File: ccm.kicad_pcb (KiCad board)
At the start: 2 copper layers, 80.1 x 75.2 mm, 24 parts, among them J3 Conn_01x04_Socket, J4 Conn_01x04_Socket, J5 Conn_01x04_Socket, J6 Conn_01x02_Socket, J7 Conn_01x02_Socket, J8 Conn_01x04_Socket, U1 Teensy4.1, U2 LM1117DT-1.8, U3 SN65HVD230, U4 SN65HVD230

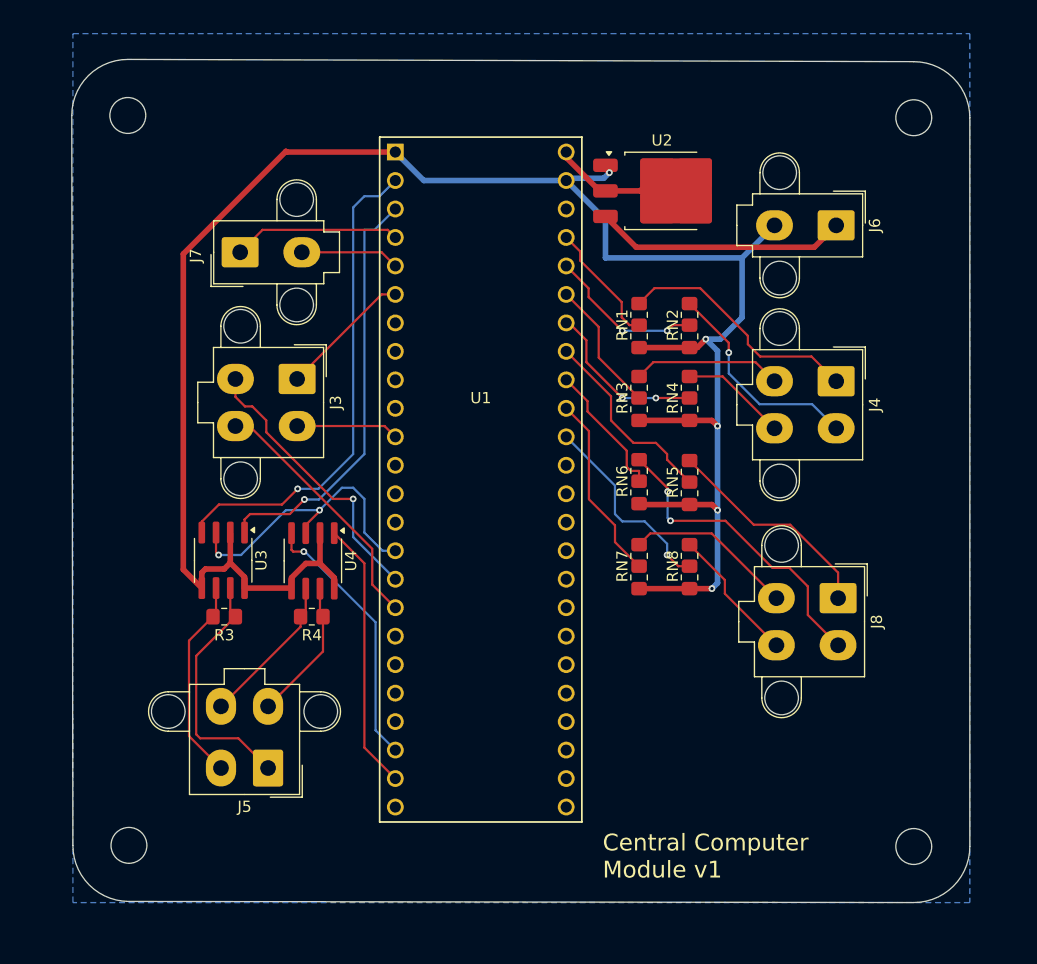
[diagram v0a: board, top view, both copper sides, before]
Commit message: add mosfet for brake light output and decoupling capacitors
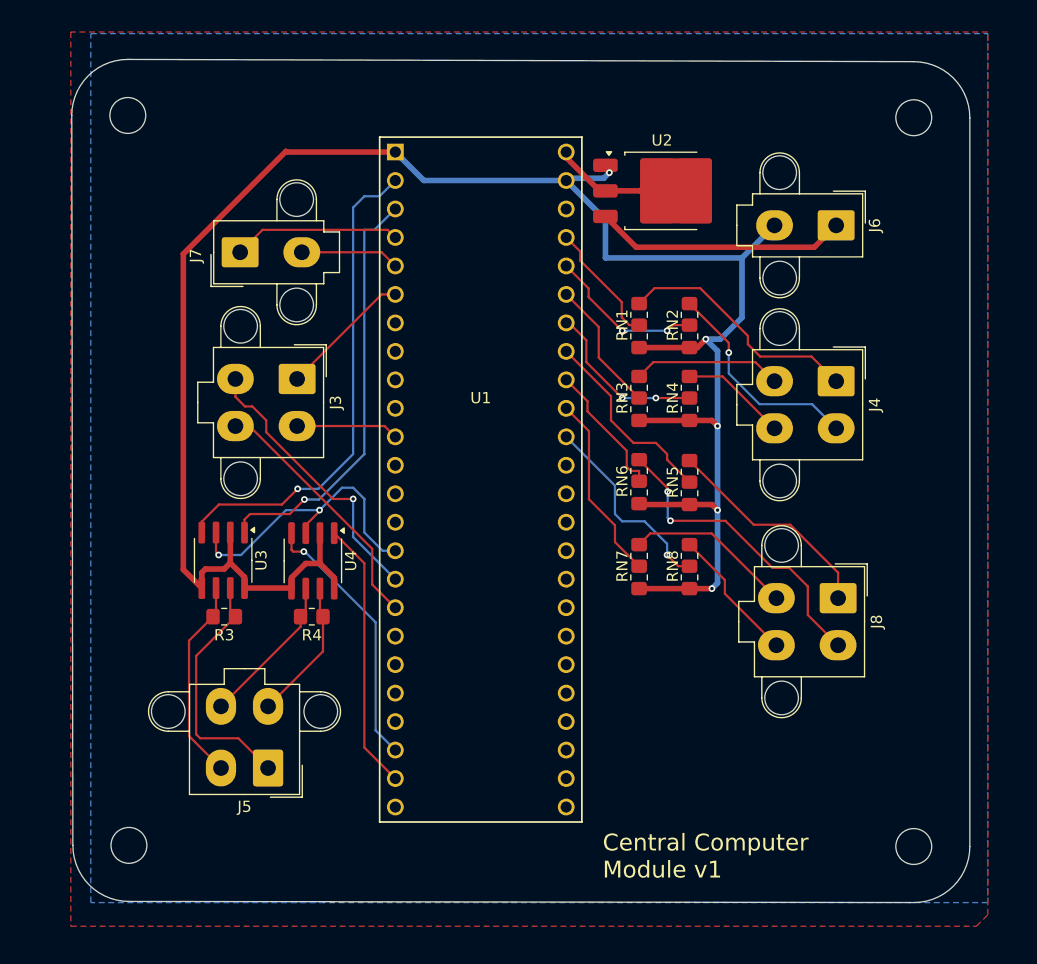
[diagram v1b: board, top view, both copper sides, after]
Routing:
- added copper zone on F.Cu, net GLV-
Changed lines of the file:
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@@
+		(net 2)
+		(net_name "GLV-")
+		(layer "F.Cu")
+		(hatch edge 0.5)
+		(priority 1)
+		(connect_pads
+			(clearance 0.5)
+		)
+		(min_thickness 0.25)
+		(filled_areas_thickness no)
+		(fill yes
+			(thermal_gap 0.5)
+			(thermal_bridge_width 0.5)
+		)
+		(polygon
+			(pts
+				(xy 108.816 59.356) (xy 108.816 139.112) (xy 189.588 139.112) (xy 190.604 138.096) (xy 190.604 59.356)
+			)
+		)
+	)
+	(zone
 		(net 2)
 		(net_name "GLV-")
@@
 		(polygon
 			(pts
-				(xy 109 59.5) (xy 189 59.5) (xy 189 137) (xy 109 137)
+				(xy 110.604 59.5) (xy 190.604 59.5) (xy 190.604 137) (xy 110.604 137)
 			)
 		)

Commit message: backup commit (no split termination or speaker amp)
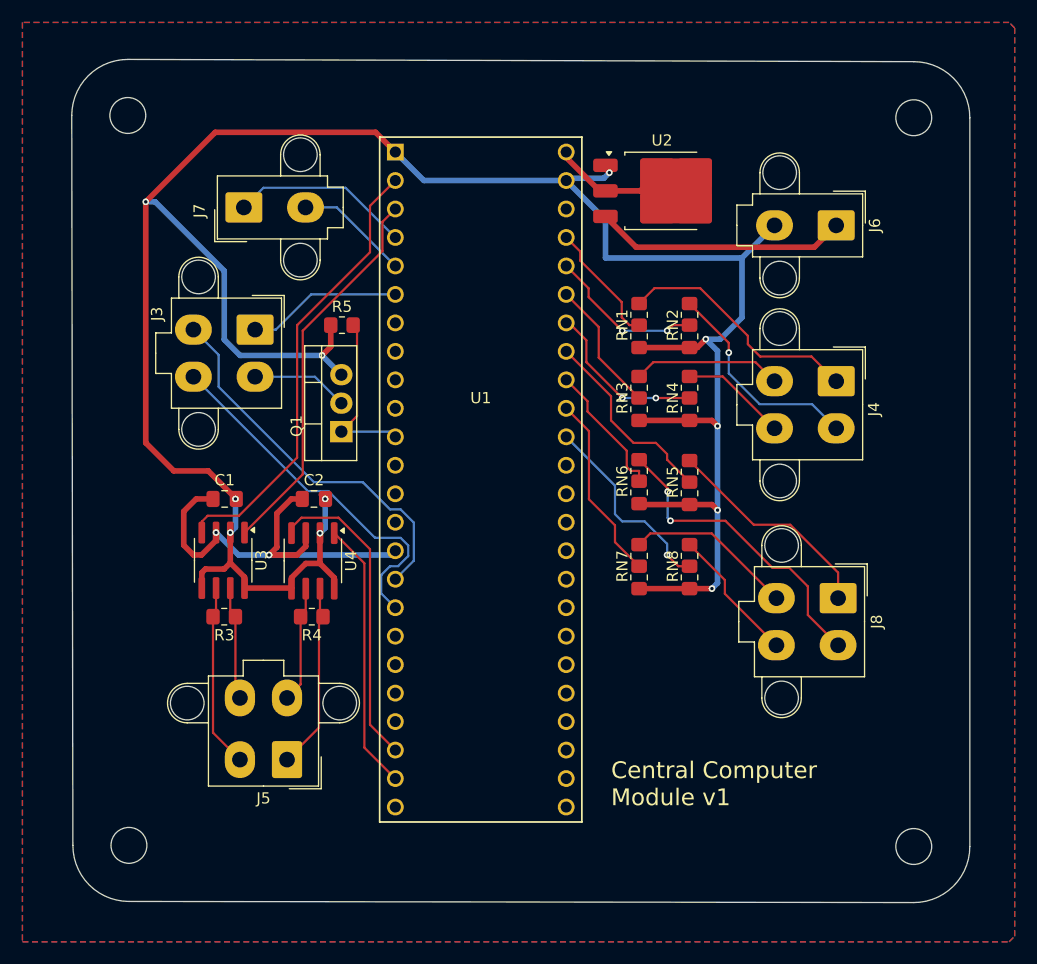
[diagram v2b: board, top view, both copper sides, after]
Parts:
- added C1: 100 nF, Capacitor_SMD:C_0805_2012Metric_Pad1.18x1.45mm_HandSolder, F.Cu at (122.5, 101.0)
- added C2: 100 nF, Capacitor_SMD:C_0805_2012Metric_Pad1.18x1.45mm_HandSolder, F.Cu at (130.5, 101.0)
- added Q1: IRLZ34N, Package_TO_SOT_THT:TO-220-3_Vertical, F.Cu at (132.9, 95.0)
- added R5: 10k, Resistor_SMD:R_0805_2012Metric_Pad1.20x1.40mm_HandSolder, F.Cu at (133.0, 85.5)
- U2: value LM1117DT-1.8 -> LM1117DT-5.0
- moved J3 5.78 mm to (125.2, 85.9)
- moved J7 4.01 mm to (124.2, 75.0)
- moved J5 1.85 mm to (128.1, 124.2)
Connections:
- J5 pad 1: CANH_1 -> CANH_2
- J5 pad 3: CANH_2 -> CANL_2
- J5 pad 4: CANL_2 -> CANH_1
- U1 pad 11: brake_light -> Net-(Q1-G)
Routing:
- net GLV-: track 181.9 -> 223.5 mm, vias 5 -> 11
- net Net-(Q1-G): track 0.00 -> 15.2 mm
- net CANH_1: track 22.3 -> 10.2 mm
- net +3.3V: track 27.0 -> 39.1 mm
- net i2c_SDA: track 22.8 -> 32.9 mm
- net i2c_SCL: track 25.2 -> 34.2 mm, vias 1 -> 0
- net CAN_RX_2: track 23.8 -> 27.9 mm, vias 1 -> 0
- net CANH_2: track 12.6 -> 16.7 mm
- net CAN_RX_1: track 43.7 -> 40.2 mm, vias 1 -> 0
- net CAN_TX_1: track 37.8 -> 34.4 mm, vias 1 -> 0
- net CANL_2: track 13.6 -> 10.4 mm
- net ready_to_drive_button: track 11.9 -> 13.8 mm
- net CANL_1: track 18.2 -> 16.4 mm
- net PWM_in_2: track 8.85 -> 10.2 mm
- net PWM_in_1: track 15.0 -> 16.1 mm

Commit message: changed voltage divider to use 2 resistors
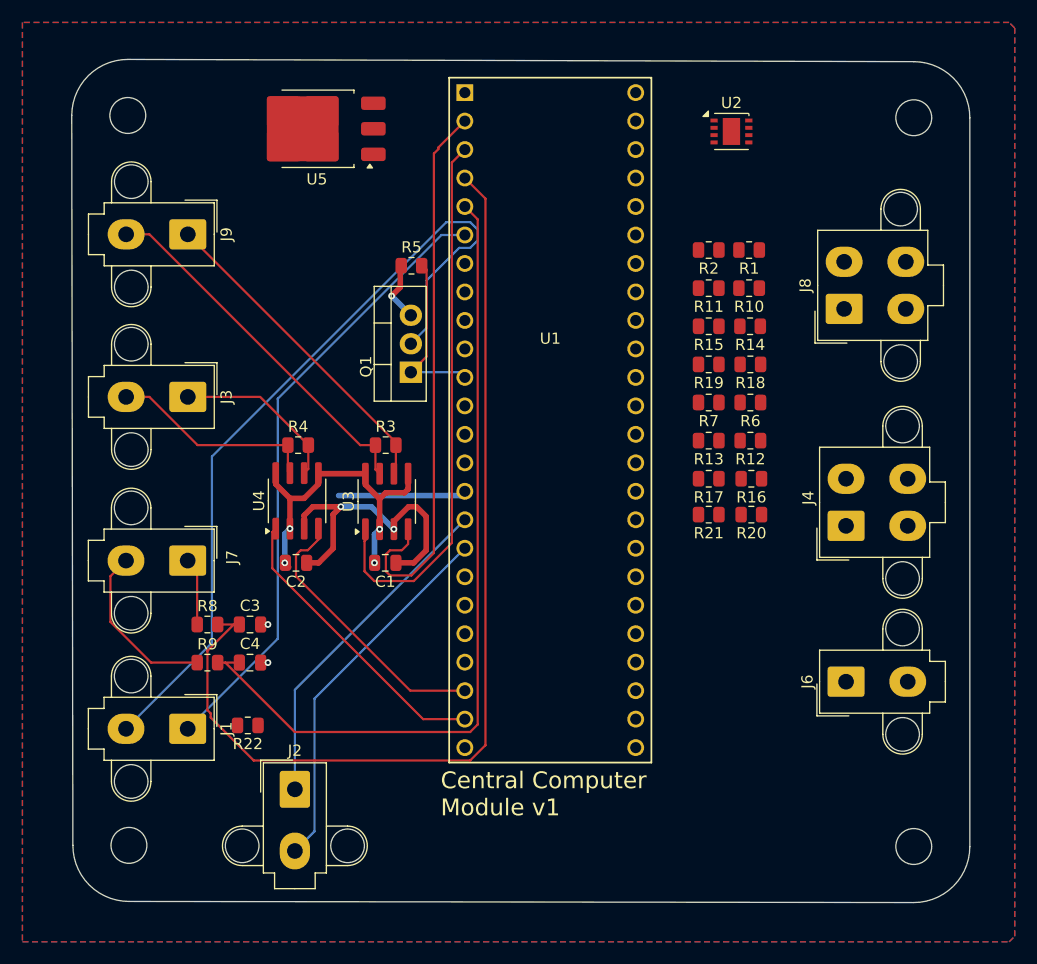
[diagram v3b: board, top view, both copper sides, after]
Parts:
- removed J5: Conn_01x04_Socket, Connector_Molex:Molex_Mini-Fit_Jr_5566-04A2_2x02_P4.20mm_Vertical
- removed RN1, RN2, RN3, RN4, RN5, RN6, RN7, RN8: VoltageDivider, voltagedivider:Voltage_Divider
- added C3: 0.01uF, Capacitor_SMD:C_0805_2012Metric, F.Cu at (124.8, 112.2)
- added C4: 0.01uF, Capacitor_SMD:C_0805_2012Metric, F.Cu at (124.8, 115.6)
- added J1: Conn_01x02_Socket, Connector_Molex:Molex_Mini-Fit_Jr_5566-02A2_2x01_P4.20mm_Vertical, F.Cu at (119.2, 121.5)
- added J2: Conn_01x02_Socket, Connector_Molex:Molex_Mini-Fit_Jr_5566-02A2_2x01_P4.20mm_Vertical, F.Cu at (128.8, 126.9)
- added J9: Conn_01x02_Socket, Connector_Molex:Molex_Mini-Fit_Jr_5566-02A2_2x01_P4.20mm_Vertical, F.Cu at (119.2, 77.4)
- added R1: 1k, Resistor_SMD:R_0805_2012Metric, F.Cu at (169.3, 78.8)
- added R10: 1k, Resistor_SMD:R_0805_2012Metric, F.Cu at (169.3, 82.2)
- added R11: 1k, Resistor_SMD:R_0805_2012Metric, F.Cu at (165.7, 82.2)
- added R12: 1k, Resistor_SMD:R_0805_2012Metric, F.Cu at (169.4, 95.8)
- added R13: 1k, Resistor_SMD:R_0805_2012Metric, F.Cu at (165.7, 95.8)
- added R14: 1k, Resistor_SMD:R_0805_2012Metric, F.Cu at (169.4, 85.6)
- added R15: 1k, Resistor_SMD:R_0805_2012Metric, F.Cu at (165.7, 85.6)
- added R16: 1k, Resistor_SMD:R_0805_2012Metric, F.Cu at (169.5, 99.2)
- added R17: 1k, Resistor_SMD:R_0805_2012Metric, F.Cu at (165.7, 99.2)
- added R18: 1k, Resistor_SMD:R_0805_2012Metric, F.Cu at (169.4, 89.0)
- added R19: 1k, Resistor_SMD:R_0805_2012Metric, F.Cu at (165.7, 89.0)
- added R2: 1k, Resistor_SMD:R_0805_2012Metric, F.Cu at (165.7, 78.8)
- added R20: 1k, Resistor_SMD:R_0805_2012Metric, F.Cu at (169.5, 102.4)
- added R21: 1k, Resistor_SMD:R_0805_2012Metric, F.Cu at (165.7, 102.4)
- added R22: 10k, Resistor_SMD:R_0805_2012Metric, F.Cu at (124.6, 121.2)
- added R6: 1k, Resistor_SMD:R_0805_2012Metric, F.Cu at (169.4, 92.4)
- added R7: 1k, Resistor_SMD:R_0805_2012Metric, F.Cu at (165.7, 92.4)
- added R8: 10, Resistor_SMD:R_0805_2012Metric, F.Cu at (121.0, 112.2)
- added R9: 10, Resistor_SMD:R_0805_2012Metric, F.Cu at (121.0, 115.6)
- added U5: LM1117DT-5.0, Package_TO_SOT_SMD:TO-252-3_TabPin2, F.Cu at (130.8, 68.0)
- C1, C2: footprint Capacitor_SMD:C_0805_2012Metric_Pad1.18x1.45mm_HandSolder -> Capacitor_SMD:C_0805_2012Metric
- J3: value Conn_01x04_Socket -> Conn_01x02_Socket; footprint Connector_Molex:Molex_Mini-Fit_Jr_5566-04A2_2x02_P4.20mm_Vertical -> Connector_Molex:Molex_Mini-Fit_Jr_5566-02A2_2x01_P4.20mm_Vertical
- R3, R4, R5: footprint Resistor_SMD:R_0805_2012Metric_Pad1.20x1.40mm_HandSolder -> Resistor_SMD:R_0805_2012Metric
- U2: value LM1117DT-5.0 -> PAM8302AAY; footprint Package_TO_SOT_SMD:TO-252-3_TabPin2 -> Package_DFN_QFN:DFN-8-1EP_3x3mm_P0.65mm_EP1.55x2.4mm
- moved J6 40.7 mm to (178.0, 117.3), turned to 90 degrees
- moved J7 31.9 mm to (119.2, 106.5), turned to -90 degrees
- moved J8 25.8 mm to (177.8, 84.0), turned to 90 degrees
- moved R3 21.0 mm to (136.9, 96.2), turned to 0 degrees
- moved U3 15.5 mm to (137.0, 101.2), turned to 90 degrees
- moved C1 15.4 mm to (136.9, 106.7), turned to 180 degrees
- moved R4 15.3 mm to (129.1, 96.2), turned to 0 degrees
- moved J4 12.9 mm to (178.0, 103.4), turned to 90 degrees
- moved J3 8.49 mm to (119.2, 91.9)
- moved U2 8.16 mm to (167.7, 68.2)
- moved Q1 8.16 mm to (139.1, 89.7)
- moved U1 8.16 mm to (144.0, 64.8)
- moved R5 8.16 mm to (139.2, 80.2)
- moved C2 5.92 mm to (128.9, 106.7), turned to 180 degrees
- moved U4 5.53 mm to (129.0, 101.2), turned to 90 degrees
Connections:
- J3 pad 1: ready_to_drive_button -> CANL_2
- J3 pad 2: brake_light -> CANH_2
- U1 pad 12: unconnected-(U1-10_CS_MQSR-Pad12) -> speaker_pwm
- U1 pad 4: PWM_in_1 -> Net-(U1-2_OUT2)
- U1 pad 5: PWM_in_2 -> Net-(U1-3_LRCLK2)
- U2 pad 1: GLV- -> unconnected-(U2-~{SD}-Pad1)
- U2 pad 2: +5V -> unconnected-(U2-NC-Pad2)
- U2 pad 3: Vin -> speaker_pwm
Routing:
- net GLV-: track 223.5 -> 37.3 mm, vias 11 -> 7
- net Net-(U1-2_OUT2): track 0.00 -> 89.8 mm
- net Net-(U1-3_LRCLK2): track 0.00 -> 74.0 mm
- net brake_light: track 9.23 -> 73.9 mm
- net ready_to_drive_button: track 13.8 -> 55.5 mm
- net acc_ped_2: track 27.7 -> 0.00 mm, vias 2 -> 0
- net CANH_1: track 10.2 -> 32.7 mm
- net Vin: track 22.5 -> 0.00 mm
- net lin_pot_1: track 22.0 -> 0.00 mm
- net acc_ped_1: track 19.7 -> 0.00 mm
- net lin_pot_2: track 19.3 -> 0.00 mm, vias 1 -> 0
- net Net-(U1-16_A2_RX4_SCL1): track 17.9 -> 0.00 mm, vias 1 -> 0
- net Net-(U1-19_A5_SCL): track 17.4 -> 0.00 mm
- net Net-(U1-17_A3_TX4_SDA1): track 16.8 -> 0.00 mm
- net brake_1: track 15.1 -> 0.00 mm
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
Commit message: right side routed
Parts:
- added C5: 100 nF, Capacitor_SMD:C_0805_2012Metric, F.Cu at (125.7, 95.2)
- added C6: 100 nF, Capacitor_SMD:C_0805_2012Metric, F.Cu at (125.8, 103.1)
- added J10: Conn_01x02_Socket, Connector_Molex:Molex_Mini-Fit_Jr_5566-02A2_2x01_P4.20mm_Vertical, F.Cu at (129.4, 72.6)
- added J5: Conn_01x02_Socket, Connector_Molex:Molex_Mini-Fit_Jr_5566-02A2_2x01_P4.20mm_Vertical, F.Cu at (169.7, 125.0)
- added R23: 1k, Resistor_SMD:R_0805_2012Metric, F.Cu at (168.8, 100.8)
- added R24: 1k, Resistor_SMD:R_0805_2012Metric, F.Cu at (165.1, 100.8)
- added R25: 60, Resistor_SMD:R_0805_2012Metric, F.Cu at (128.7, 93.3)
- added R26: 60, Resistor_SMD:R_0805_2012Metric, F.Cu at (128.7, 101.2)
- R3, R4: value R_US -> 60
- moved U5 39.6 mm to (170.3, 69.0), turned to 0 degrees
- moved R5 38.9 mm to (132.3, 118.5)
- moved J6 36.3 mm to (178.0, 81.0)
- moved U2 35.6 mm to (133.9, 79.5)
- moved J8 33.7 mm to (178.4, 117.8)
- moved R8 29.5 mm to (131.9, 84.8)
- moved C3 29.5 mm to (135.7, 84.8)
- moved R9 29.5 mm to (131.9, 88.2)
- moved C4 29.5 mm to (135.7, 88.2)
- moved J7 29.1 mm to (119.8, 77.5)
- moved Q1 23.9 mm to (135.0, 113.3), turned to 180 degrees
- moved R20 23.4 mm to (168.7, 79.0)
- moved R21 23.4 mm to (165.1, 79.0)
- moved J3 14.6 mm to (119.7, 106.5)
- moved J9 14.3 mm to (119.8, 91.7)
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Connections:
- J4 pad 1: lin_pot_1 -> lin_pot_4
- J4 pad 2: lin_pot_2 -> lin_pot_3
- J4 pad 3: lin_pot_3 -> lin_pot_2
- J4 pad 4: lin_pot_4 -> lin_pot_1
- J8 pad 1: acc_ped_1 -> brake_2
- J8 pad 2: acc_ped_2 -> brake_1
- J8 pad 3: brake_1 -> acc_ped_2
- J8 pad 4: brake_2 -> acc_ped_1
- R3 pad 2: CANL_1 -> Net-(C5-Pad1)
- R4 pad 2: CANL_2 -> Net-(C6-Pad1)
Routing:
- net Net-(U1-2_OUT2): track 89.8 -> 0.00 mm
- net Net-(U1-3_LRCLK2): track 74.0 -> 0.00 mm
- net brake_light: track 73.9 -> 0.00 mm
- net ready_to_drive_button: track 55.5 -> 0.00 mm
- net CAN_RX_1: track 50.1 -> 0.00 mm
- net CAN_TX_1: track 48.9 -> 0.00 mm
- net +3.3V: track 39.1 -> 0.00 mm, vias 2 -> 0
- net GLV-: track 37.3 -> 0.00 mm, vias 7 -> 0
- net acc_ped_2: track 0.00 -> 33.3 mm
- net i2c_SDA: track 33.3 -> 0.00 mm
- net CANH_1: track 32.7 -> 0.00 mm
- net acc_ped_1: track 0.00 -> 31.6 mm
- net i2c_SCL: track 30.3 -> 0.00 mm
- net CANL_1: track 29.1 -> 0.00 mm
- net CAN_TX_2: track 26.4 -> 0.00 mm
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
